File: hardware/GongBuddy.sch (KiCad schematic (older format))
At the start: 56 parts, among them J1 10103594-0001LF, J2 Conn_ARM_JTAG_SWD_10, J3 2908-05WB-MG, J4 Conn_01x10, J5 Conn_01x02, J7 Conn_Coaxial, U1 TPS7A19, U2 USBLC6-2SC6, U3 MCP73831T-2ACI_OT, U4 ST_Sensortile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

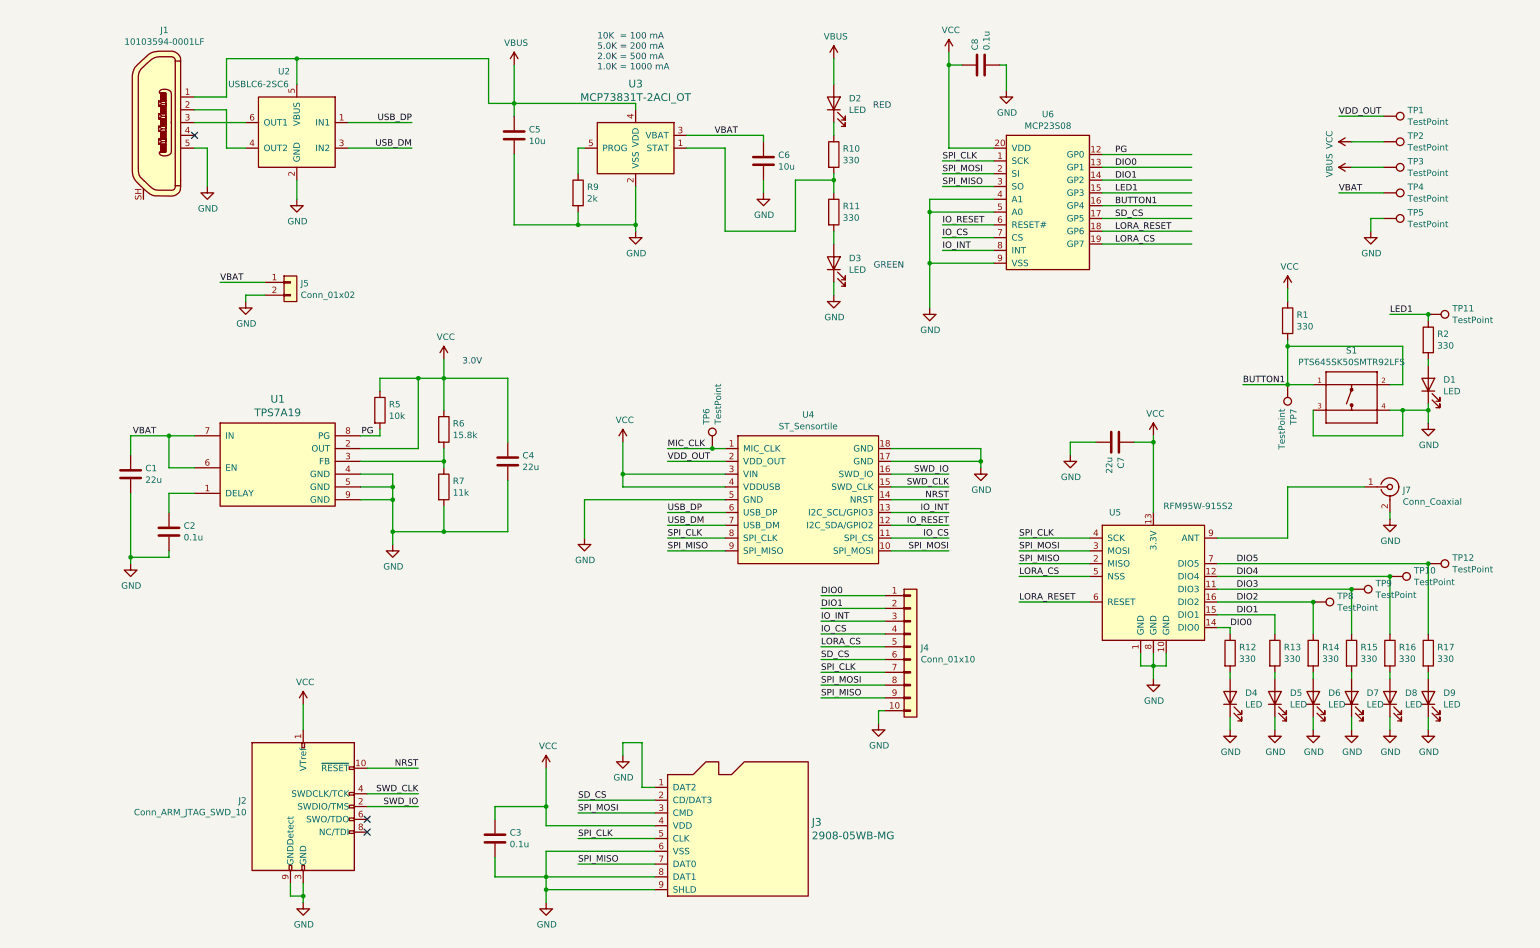
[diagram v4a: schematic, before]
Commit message: Tweaked layout based on integration with the enclosure.
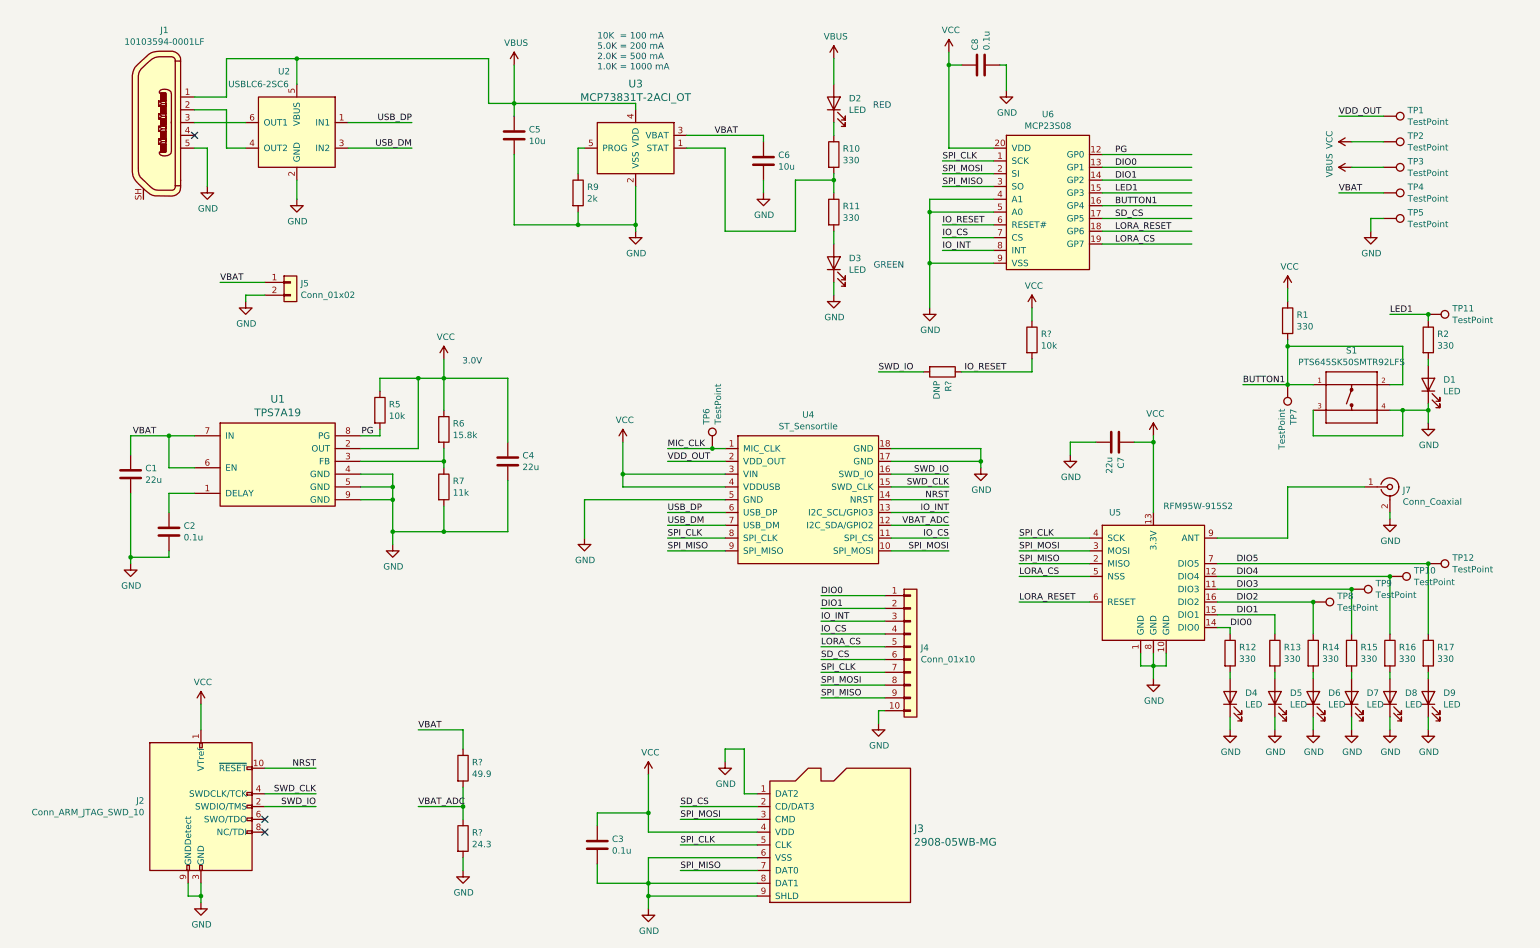
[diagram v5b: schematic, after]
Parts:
- added R?: 24.3, Resistor_SMD:R_0603_1608Metric, symbol Device:R
- added R?: 49.9, Resistor_SMD:R_0603_1608Metric, symbol Device:R
- added R?: DNP, Resistor_SMD:R_0603_1608Metric, symbol Device:R
- added R?: 10k, Resistor_SMD:R_0603_1608Metric, symbol Device:R
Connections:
- net labels added: VBAT_ADC
- wire segments 239 -> 249
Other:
- moved on the sheet: C3, J2, J3

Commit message: Added ESD diodes and cleaned up the silkscreen.
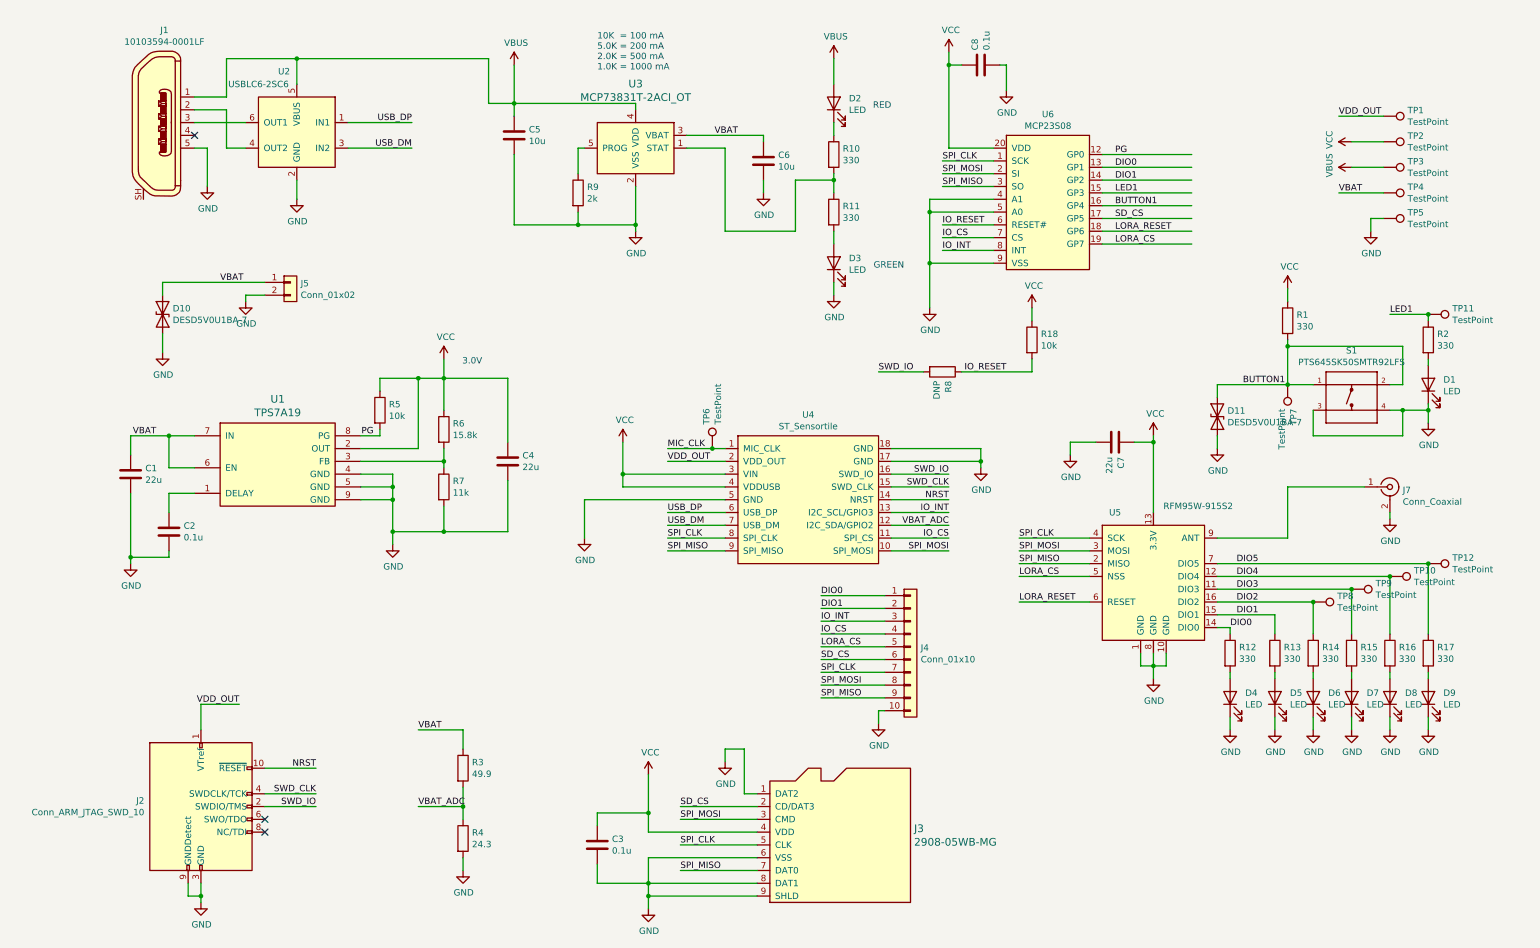
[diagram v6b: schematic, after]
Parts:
- added D10, D11: DESD5V0U1BA-7, Diode_SMD:D_SOD-323, symbol Diode:ESD9B5.0ST5G
- gave numbers to parts that had none: 4
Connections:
- wire segments 249 -> 254
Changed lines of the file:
@@
 Wire Wire Line
 	1550 2750 1550 2800
-Wire Wire Line
-	1700 2650 1350 2650
 Text Label 1350 2650 0    50   ~ 0
 VBAT
@@
 NoConn ~ 1700 6850
 NoConn ~ 1700 6950
-$Comp
-L power:VCC #PWR02
-U 1 1 60ADF77F
-P 1200 5950
-F 0 "#PWR02" H 1200 5800 50  0001 C CNN
-F 1 "VCC" H 1215 6123 50  0000 C CNN
-F 2 "" H 1200 5950 50  0001 C CNN
-F 3 "" H 1200 5950 50  0001 C CNN
-	1    1200 5950
-	1    0    0    -1
-$EndComp
 Wire Wire Line
 	1200 5950 1200 6150
@@
 Wire Wire Line
 	9700 2700 9700 2800
-Wire Wire Line
-	9350 3450 9700 3450
 Text Label 9350 3450 0    50   ~ 0
 BUTTON1
@@
 $EndComp
 $Comp
-L Device:R R?
+L Device:R R4
 U 1 1 60A65374
 P 3250 7000
-F 0 "R?" H 3320 7046 50  0000 L CNN
+F 0 "R4" H 3320 7046 50  0000 L CNN
 F 1 "24.3" H 3320 6955 50  0000 L CNN
 F 2 "Resistor_SMD:R_0603_1608Metric" V 3180 7000 50  0001 C CNN
@@
 $EndComp
 $Comp
-L Device:R R?
+L Device:R R3
 U 1 1 60A661CD
 P 3250 6450
-F 0 "R?" H 3320 6496 50  0000 L CNN
+F 0 "R3" H 3320 6496 50  0000 L CNN
 F 1 "49.9" H 3320 6405 50  0000 L CNN
 F 2 "Resistor_SMD:R_0603_1608Metric" V 3180 6450 50  0001 C CNN
@@
 $EndComp
 $Comp
-L Device:R R?
+L Device:R R8
 U 1 1 60A66623
 P 7000 3350
-F 0 "R?" H 7070 3396 50  0000 L CNN
+F 0 "R8" H 7070 3396 50  0000 L CNN
 F 1 "DNP" H 7070 3305 50  0000 L CNN
 F 2 "Resistor_SMD:R_0603_1608Metric" V 6930 3350 50  0001 C CNN
@@
 IO_RESET
 $Comp
-L Device:R R?
+L Device:R R18
 U 1 1 60A95B7B
 P 7700 3100
-F 0 "R?" H 7770 3146 50  0000 L CNN
+F 0 "R18" H 7770 3146 50  0000 L CNN
 F 1 "10k" H 7770 3055 50  0000 L CNN
 F 2 "Resistor_SMD:R_0603_1608Metric" V 7630 3100 50  0001 C CNN
@@
 $EndComp
 $Comp
-L power:VCC #PWR?
+L power:VCC #PWR038
 U 1 1 60A962A7
 P 7700 2850
-F 0 "#PWR?" H 7700 2700 50  0001 C CNN
+F 0 "#PWR038" H 7700 2700 50  0001 C CNN
 F 1 "VCC" H 7715 3023 50  0000 C CNN
 F 2 "" H 7700 2850 50  0001 C CNN
@@
 	3250 6750 3250 6850
 $Comp
-L power:GND #PWR?
+L power:GND #PWR037
 U 1 1 60AE51B9
 P 3250 7250
-F 0 "#PWR?" H 3250 7000 50  0001 C CNN
+F 0 "#PWR037" H 3250 7000 50  0001 C CNN
 F 1 "GND" H 3255 7077 50  0000 C CNN
 F 2 "" H 3250 7250 50  0001 C CNN
@@
 Text Label 2900 6750 0    50   ~ 0
 VBAT_ADC
+Wire Wire Line
+	900  2650 900  2750
+Wire Wire Line
+	900  2650 1700 2650
+$Comp
+L power:GND #PWR036
+U 1 1 60A753BD
+P 900 3200
+F 0 "#PWR036" H 900 2950 50  0001 C CNN
+F 1 "GND" H 905 3027 50  0000 C CNN
+F 2 "" H 900 3200 50  0001 C CNN
+F 3 "" H 900 3200 50  0001 C CNN
+	1    900  3200
+	1    0    0    -1
+$EndComp
+Wire Wire Line
+	900  3050 900  3200
+$Comp
+L Diode:ESD9B5.0ST5G D11
+U 1 1 60A861EF
+P 9150 3700
+F 0 "D11" V 9104 3779 50  0000 L CNN
+F 1 "DESD5V0U1BA-7" V 9195 3779 50  0000 L CNN
+F 2 "Diode_SMD:D_SOD-323" H 9150 3700 50  0001 C CNN
+F 3 "https://www.onsemi.com/pub/Collateral/ESD9B-D.PDF" H 9150 3700 50  0001 C CNN
+	1    9150 3700
+	0    1    1    0
+$EndComp
+Wire Wire Line
+	9150 3550 9150 3450
+Wire Wire Line
+	9150 3450 9700 3450
+$Comp
+L power:GND #PWR039
+U 1 1 60A986EE
+P 9150 3950
+F 0 "#PWR039" H 9150 3700 50  0001 C CNN
+F 1 "GND" H 9155 3777 50  0000 C CNN
+F 2 "" H 9150 3950 50  0001 C CNN
+F 3 "" H 9150 3950 50  0001 C CNN
+	1    9150 3950
+	1    0    0    -1
+$EndComp
+Wire Wire Line
+	9150 3850 9150 3950
+$Comp
+L Diode:ESD9B5.0ST5G D10
+U 1 1 60AAE0CA
+P 900 2900
+F 0 "D10" V 854 2979 50  0000 L CNN
+F 1 "DESD5V0U1BA-7" V 945 2979 50  0000 L CNN
+F 2 "Diode_SMD:D_SOD-323" H 900 2900 50  0001 C CNN
+F 3 "https://www.onsemi.com/pub/Collateral/ESD9B-D.PDF" H 900 2900 50  0001 C CNN
+	1    900  2900
+	0    1    1    0
+$EndComp
+Wire Wire Line
+	1200 5950 1500 5950
+Text Label 1500 5950 2    50   ~ 0
+VDD_OUT
 $EndSCHEMATC

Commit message: Tweaked the RF lines.
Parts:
- D10, D11: Digi-Key_PN (none) -> DESD5V0U1BA-7DITR-ND
- S1: Digi-Key_PN (none) -> CKN9087CT-ND; MANUFACTURER CnK -> (none); MPN (none) -> PTS645SK50SMTR92 LFS; Manufacturer (none) -> CnK
- U1: Digi-Key_PN (none) -> 296-45026-1-ND; MPN (none) -> TPS7A1901DRBT; Manufacturer (none) -> Texas Instruments
- U2: Digi-Key_PN (none) -> 497-5235-2-ND; Digikey 497-5235-2-ND -> (none); MPN (none) -> DESD5V0U1BA-7; Manufacturer (none) -> Diodes Incorporated
- U6: Digi-Key_PN (none) -> MCP23S08T-E/SOTR-ND; MPN (none) -> MCP23S08T-E/SO; Manufacturer (none) -> Microchip Technology
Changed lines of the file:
@@
 F 2 "Package_TO_SOT_SMD:SOT-23-6" H 1950 1500 50  0001 C CNN
 F 3 "" H 1950 1500 50  0001 C CNN
-F 4 "497-5235-2-ND" H 1950 1500 50  0001 C CNN "Digikey"
+F 4 "" H 1950 1500 50  0001 C CNN "Digikey"
+F 5 "497-5235-2-ND" H 1950 1500 50  0001 C CNN "Digi-Key_PN"
+F 6 "DESD5V0U1BA-7" H 1950 1500 50  0001 C CNN "MPN"
+F 7 "Diodes Incorporated" H 1950 1500 50  0001 C CNN "Manufacturer"
 	1    1950 1500
 	-1   0    0    -1
@@
 F 2 "KicadFootprint:IC_DRV8601DRBT" H 1800 4000 60  0001 C CNN
 F 3 "" H 1800 4000 60  0001 C CNN
+F 4 "296-45026-1-ND" H 1800 4000 50  0001 C CNN "Digi-Key_PN"
+F 5 "TPS7A1901DRBT" H 1800 4000 50  0001 C CNN "MPN"
+F 6 "Texas Instruments" H 1800 4000 50  0001 C CNN "Manufacturer"
 	1    1800 4000
 	1    0    0    -1
@@
 F 2 "Package_SO:SSOP-20_5.3x7.2mm_P0.65mm" H 7800 2000 50  0001 C CNN
 F 3 "" H 7800 2000 50  0001 C CNN
+F 4 "MCP23S08T-E/SOTR-ND" H 7800 2000 50  0001 C CNN "Digi-Key_PN"
+F 5 "MCP23S08T-E/SO" H 7800 2000 50  0001 C CNN "MPN"
+F 6 "Microchip Technology" H 7800 2000 50  0001 C CNN "Manufacturer"
 	1    7800 2000
 	1    0    0    -1
@@
 F 3 "" H 10200 3550 50  0001 L BNN
 F 4 "Manufacturer Recommendations" H 10200 3550 50  0001 L BNN "STANDARD"
-F 5 "CnK" H 10200 3550 50  0001 L BNN "MANUFACTURER"
+F 5 "" H 10200 3550 50  0001 L BNN "MANUFACTURER"
+F 6 "CKN9087CT-ND" H 10200 3550 50  0001 C CNN "Digi-Key_PN"
+F 7 "PTS645SK50SMTR92 LFS" H 10200 3550 50  0001 C CNN "MPN"
+F 8 "CnK" H 10200 3550 50  0001 C CNN "Manufacturer"
 	1    10200 3550
 	1    0    0    -1
@@
 F 2 "Diode_SMD:D_SOD-323" H 9150 3700 50  0001 C CNN
 F 3 "https://www.onsemi.com/pub/Collateral/ESD9B-D.PDF" H 9150 3700 50  0001 C CNN
+F 4 "DESD5V0U1BA-7DITR-ND" H 9150 3700 50  0001 C CNN "Digi-Key_PN"
 	1    9150 3700
 	0    1    1    0
@@
 F 2 "Diode_SMD:D_SOD-323" H 900 2900 50  0001 C CNN
 F 3 "https://www.onsemi.com/pub/Collateral/ESD9B-D.PDF" H 900 2900 50  0001 C CNN
+F 4 "DESD5V0U1BA-7DITR-ND" H 900 2900 50  0001 C CNN "Digi-Key_PN"
 	1    900  2900
 	0    1    1    0
